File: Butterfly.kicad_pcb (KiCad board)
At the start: 2 copper layers, 93.1 x 65.5 mm, 28 parts, among them J1 Conn_02x03_Odd_Even, J2 USB_A, U1 ATTINY85-20PU

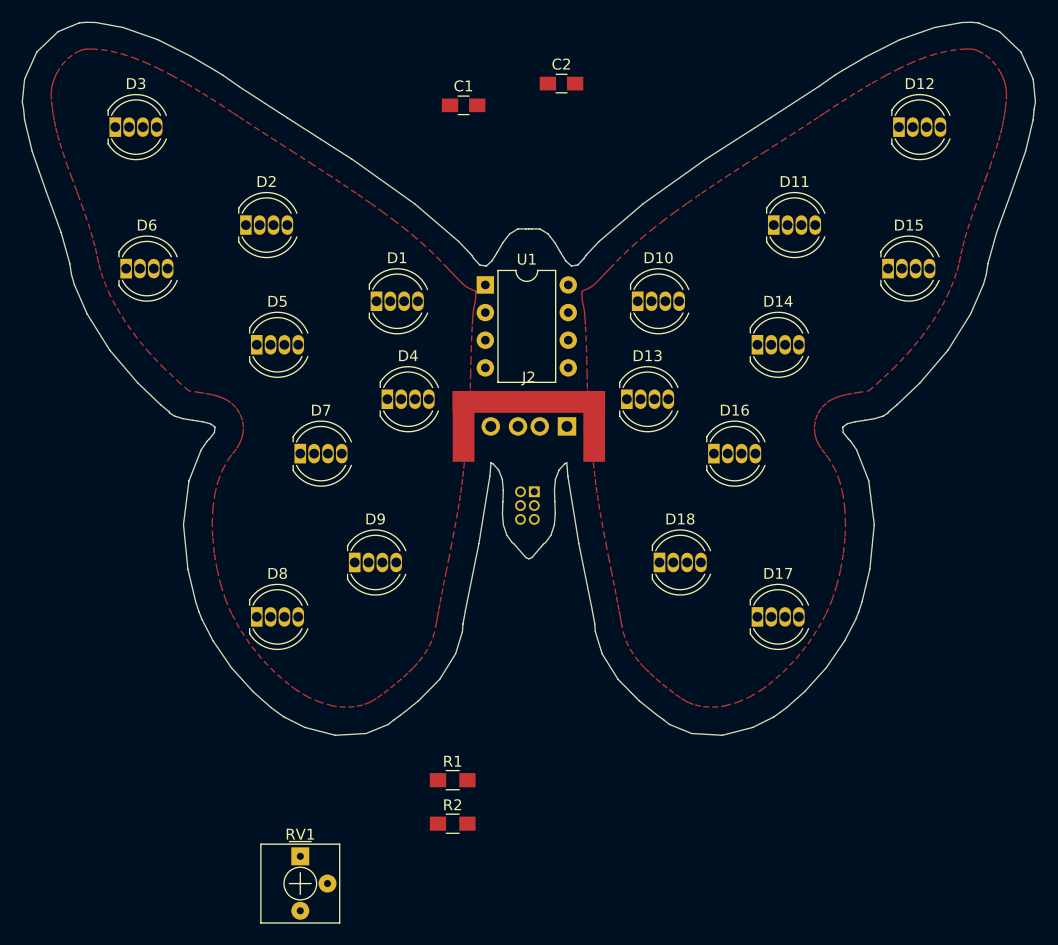
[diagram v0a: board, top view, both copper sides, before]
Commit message: Position SMT footprints.
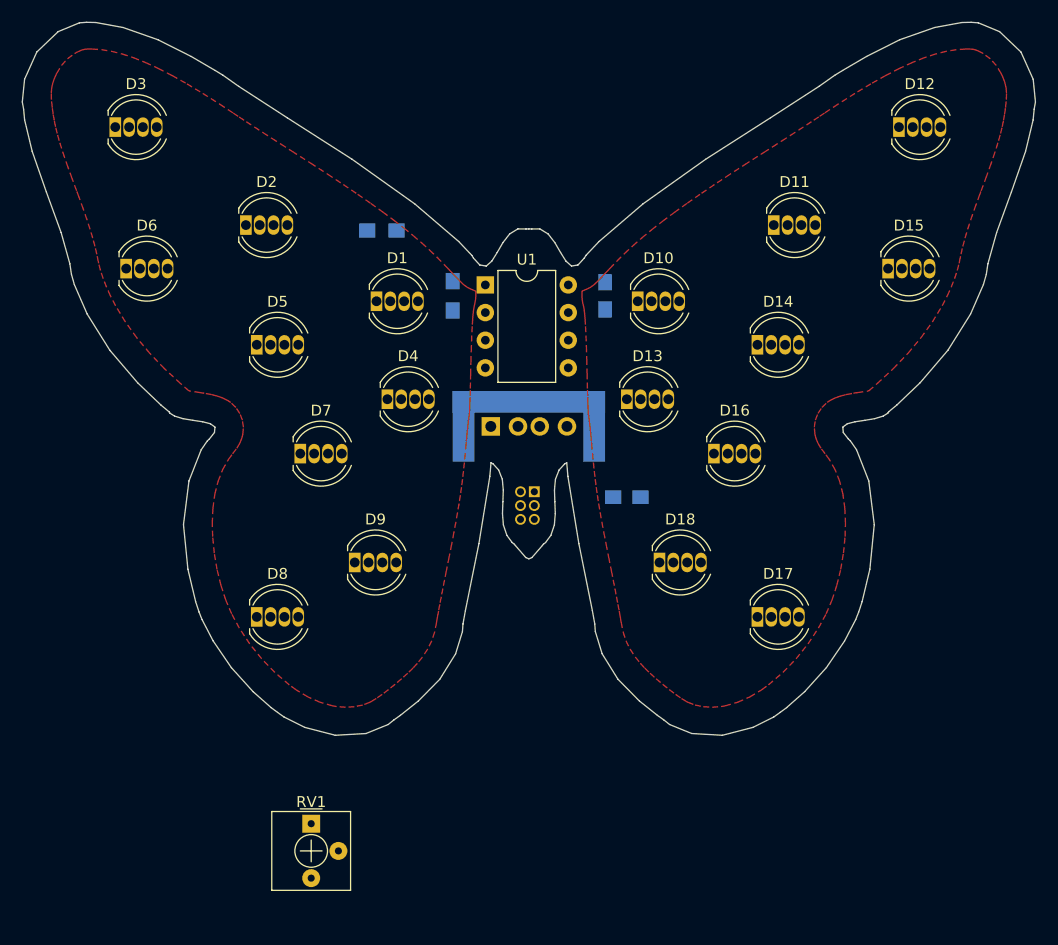
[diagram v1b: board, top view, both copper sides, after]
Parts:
- C1, C2, J2, R1, R2: moved to B.Cu
- moved R1 50.9 mm to (131.5, 88.5)
- moved R2 48.5 mm to (138.0, 94.5), turned to 270 degrees
- moved C2 38.5 mm to (154.0, 113.0)
- moved C1 21.8 mm to (152.0, 94.5), turned to 270 degrees
- moved RV1 3.16 mm to (125.0, 143.0)
- turned J2 to 180 degrees

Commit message: Use front wing zones for +5V.
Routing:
- added copper zone on F.Cu, net +5V
- removed copper zone on F.Cu, net (none)
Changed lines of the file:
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@@
   (gr_line (start 161.23777 81.9574) (end 167.20467 78.1404) (layer Edge.Cuts) (width 0.1))
   (gr_line (start 183.5 99.5) (end 180.94377 102.4917) (layer Edge.Cuts) (width 0.1))
-  (zone (net 0) (net_name "") (layer F.Cu) (hatch edge 0.508)
+  (zone (net 1) (net_name +5V) (layer F.Cu) (hatch edge 0.508)
     (connect_pads (clearance 0.508))
     (min_thickness 0.254)
@@
     )
   )
-  (zone (net 0) (net_name "") (layer F.Cu) (hatch edge 0.508)
+  (zone (net 1) (net_name +5V) (layer F.Cu) (hatch edge 0.508)
     (connect_pads (clearance 0.508))
     (min_thickness 0.254)

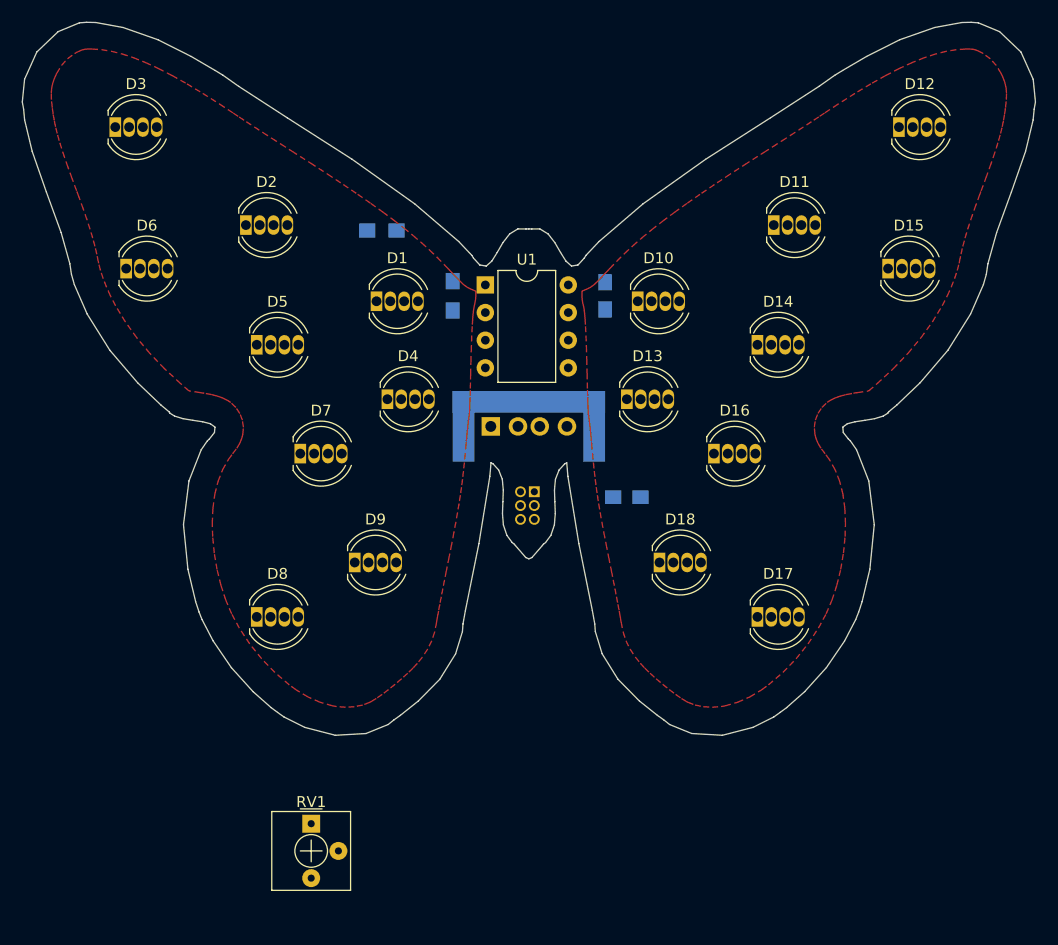
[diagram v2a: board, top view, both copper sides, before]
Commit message: Add GND zone on back.
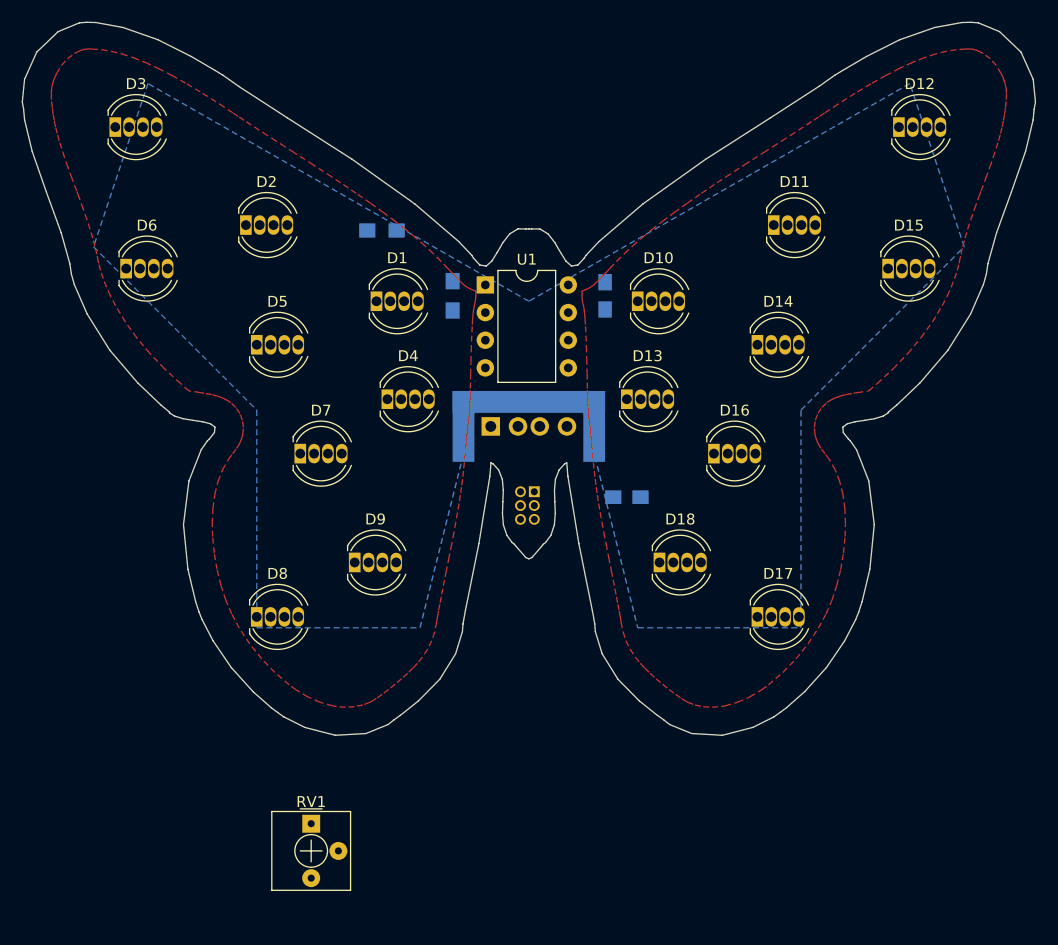
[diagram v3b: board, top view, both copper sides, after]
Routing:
- added copper zone on B.Cu, net GND
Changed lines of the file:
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@@
+    )
+  )
+  (zone (net 2) (net_name GND) (layer B.Cu) (hatch edge 0.508)
+    (connect_pads (clearance 0.508))
+    (min_thickness 0.254)
+    (fill (arc_segments 16) (thermal_gap 0.508) (thermal_bridge_width 0.508))
+    (polygon
+      (pts
+        (xy 145 95) (xy 110 75) (xy 105 90) (xy 120 105) (xy 120 125)
+        (xy 135 125) (xy 140 105) (xy 150 105) (xy 155 125) (xy 170 125)
+        (xy 170 105) (xy 185 90) (xy 180 75) (xy 145 95)
+      )
     )
   )

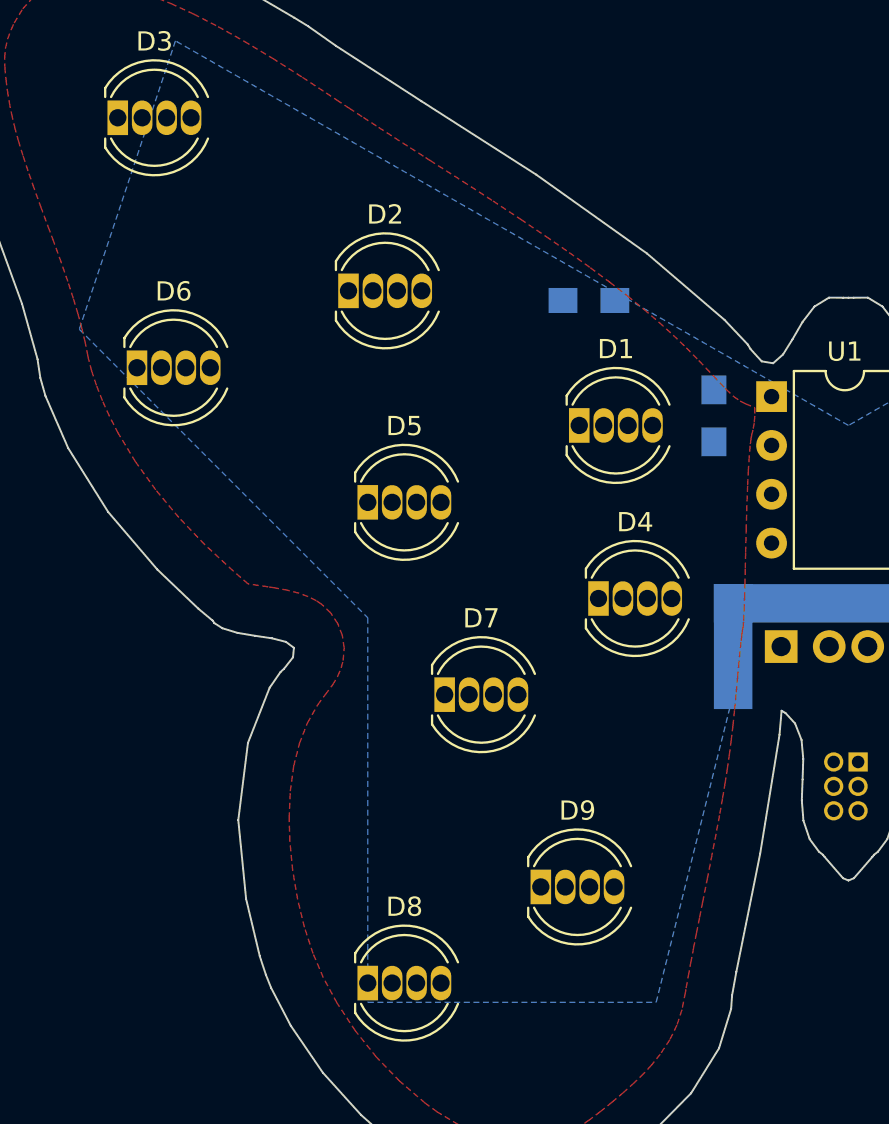
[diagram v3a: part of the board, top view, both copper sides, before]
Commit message: Draw traces on left wing.
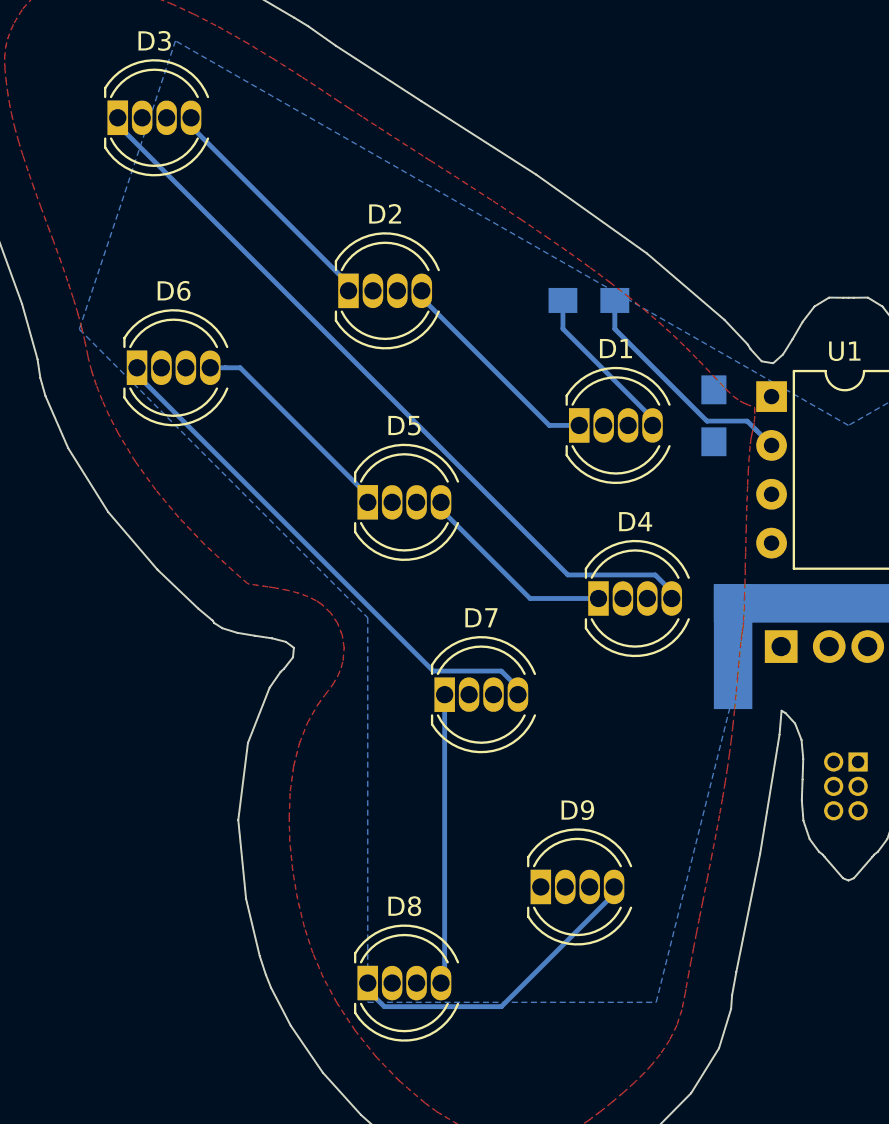
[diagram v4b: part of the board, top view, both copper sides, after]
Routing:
- net Net-(D3-Pad1): track 0.00 -> 39.6 mm
- net Net-(D6-Pad1): track 0.00 -> 27.3 mm
- net Net-(D8-Pad1): track 0.00 -> 16.3 mm
- net Net-(D7-Pad1): track 0.00 -> 15.1 mm
- net Net-(D2-Pad1): track 0.00 -> 12.4 mm
- net Net-(R1-Pad2): track 0.00 -> 12.1 mm
- net Net-(D1-Pad1): track 0.00 -> 11.3 mm
- net Net-(D5-Pad1): track 0.00 -> 11.3 mm
- net Net-(D4-Pad1): track 0.00 -> 10.5 mm
- net Net-(D1-Pad4): track 0.00 -> 8.43 mm
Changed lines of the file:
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@@
     (thickness 1.6)
     (drawings 182)
-    (tracks 0)
+    (tracks 38)
     (zones 0)
     (modules 28)
@@
   (gr_line (start 161.23777 81.9574) (end 167.20467 78.1404) (layer Edge.Cuts) (width 0.1))
   (gr_line (start 183.5 99.5) (end 180.94377 102.4917) (layer Edge.Cuts) (width 0.1))
+  (segment (start 131 95) (end 129.445 95) (width 0.25) (layer B.Cu) (net 3))
+  (segment (start 129.445 95) (end 122.81 88.365) (width 0.25) (layer B.Cu) (net 3))
+  (segment (start 122.81 88.365) (end 122.81 88) (width 0.25) (layer B.Cu) (net 3))
+  (segment (start 130.15 88.5) (end 130.15 89.975) (width 0.25) (layer B.Cu) (net 4))
+  (segment (start 130.15 89.975) (end 134.81 94.635) (width 0.25) (layer B.Cu) (net 4))
+  (segment (start 134.81 94.635) (end 134.81 95) (width 0.25) (layer B.Cu) (net 4))
+  (segment (start 119 88) (end 119 87.635) (width 0.25) (layer B.Cu) (net 5))
+  (segment (start 119 87.635) (end 110.81 79.445) (width 0.25) (layer B.Cu) (net 5))
+  (segment (start 110.81 79.445) (end 110.81 79) (width 0.25) (layer B.Cu) (net 5))
+  (segment (start 107 79) (end 107 79.365) (width 0.25) (layer B.Cu) (net 6))
+  (segment (start 107 79.365) (end 130.40999 102.77499) (width 0.25) (layer B.Cu) (net 6))
+  (segment (start 130.40999 102.77499) (end 134.94999 102.77499) (width 0.25) (layer B.Cu) (net 6))
+  (segment (start 134.94999 102.77499) (end 135.81 103.635) (width 0.25) (layer B.Cu) (net 6))
+  (segment (start 135.81 103.635) (end 135.81 104) (width 0.25) (layer B.Cu) (net 6))
+  (segment (start 132 104) (end 128.445 104) (width 0.25) (layer B.Cu) (net 7))
+  (segment (start 128.445 104) (end 123.81 99.365) (width 0.25) (layer B.Cu) (net 7))
+  (segment (start 123.81 99.365) (end 123.81 99) (width 0.25) (layer B.Cu) (net 7))
+  (segment (start 120 99) (end 120 98.635) (width 0.25) (layer B.Cu) (net 8))
+  (segment (start 120 98.635) (end 113.365 92) (width 0.25) (layer B.Cu) (net 8))
+  (segment (start 113.365 92) (end 112.595 92) (width 0.25) (layer B.Cu) (net 8))
+  (segment (start 112.595 92) (end 111.81 92) (width 0.25) (layer B.Cu) (net 8))
+  (segment (start 108 92) (end 108 92.365) (width 0.25) (layer B.Cu) (net 9))
+  (segment (start 108 92.365) (end 123.40999 107.77499) (width 0.25) (layer B.Cu) (net 9))
+  (segment (start 123.40999 107.77499) (end 126.94999 107.77499) (width 0.25) (layer B.Cu) (net 9))
+  (segment (start 126.94999 107.77499) (end 127.81 108.635) (width 0.25) (layer B.Cu) (net 9))
+  (segment (start 127.81 108.635) (end 127.81 109) (width 0.25) (layer B.Cu) (net 9))
+  (segment (start 124 109) (end 124 123.81) (width 0.25) (layer B.Cu) (net 10))
+  (segment (start 124 123.81) (end 123.81 124) (width 0.25) (layer B.Cu) (net 10))
+  (segment (start 120 124) (end 120 124.365) (width 0.25) (layer B.Cu) (net 11))
+  (segment (start 120 124.365) (end 120.86001 125.22501) (width 0.25) (layer B.Cu) (net 11))
+  (segment (start 120.86001 125.22501) (end 126.94999 125.22501) (width 0.25) (layer B.Cu) (net 11))
+  (segment (start 126.94999 125.22501) (end 132.81 119.365) (width 0.25) (layer B.Cu) (net 11))
+  (segment (start 132.81 119.365) (end 132.81 119) (width 0.25) (layer B.Cu) (net 11))
+  (segment (start 132.85 88.5) (end 132.85 89.985002) (width 0.25) (layer B.Cu) (net 28))
+  (segment (start 132.85 89.985002) (end 137.639997 94.774999) (width 0.25) (layer B.Cu) (net 28))
+  (segment (start 137.639997 94.774999) (end 139.734999 94.774999) (width 0.25) (layer B.Cu) (net 28))
+  (segment (start 139.734999 94.774999) (end 140.200001 95.240001) (width 0.25) (layer B.Cu) (net 28))
+  (segment (start 140.200001 95.240001) (end 141 96.04) (width 0.25) (layer B.Cu) (net 28))
   (zone (net 1) (net_name +5V) (layer F.Cu) (hatch edge 0.508)
     (connect_pads (clearance 0.508))
